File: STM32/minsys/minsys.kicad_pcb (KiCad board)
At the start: 2 copper layers, 29 parts, among them J1 USB_B_Micro, J2 ST-LINK, J3 BOOT, J4 Conn_01x20, J5 Conn_01x20, SW1 RST, U1 STM32F103C8Tx, U2 AMS1117-3.3, Y1 8MHz, Y2 32.758K

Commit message: edit pcb
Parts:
- D2: footprint LED_SMD:LED_0402_1005Metric_Pad0.77x0.64mm_HandSolder -> LED_SMD:LED_0603_1608Metric_Pad1.05x0.95mm_HandSolder
- moved R3 12.8 mm to (224.2, 76.0)
- moved R4 11.7 mm to (226.7, 35.2), turned to 180 degrees
- moved C8 4.05 mm to (234.6, 39.6)
- moved R2 3.89 mm to (230.9, 77.2), turned to -90 degrees
- moved D1 2.65 mm to (238.9, 34.3)
- moved R1 1.42 mm to (228.1, 77.2), turned to -90 degrees
- moved J2 0.88 mm to (230.2, 31.6)
- moved D2 0.28 mm to (217.4, 66.7)
- moved R5 0.26 mm to (234.9, 32.8)
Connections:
- C6 pad 1: RTCIN -> PC14
- C7 pad 1: RTCOUT -> PC15
- U1 pad 3: RTCIN -> PC14
- U1 pad 4: RTCOUT -> PC15
- Y2 pad 1: RTCIN -> PC14
- Y2 pad 2: RTCOUT -> PC15
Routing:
- net PC14: track 0.00 -> 41.1 mm
- net PC15: track 0.00 -> 36.6 mm
- net PC13: track 8.62 -> 42.6 mm
- net RTCIN: track 21.2 -> 0.00 mm
- net RTCOUT: track 18.1 -> 0.00 mm
- net Net-(J1-D-): track 0.00 -> 9.83 mm
- net SWDIO: track 0.00 -> 8.70 mm, vias 0 -> 1
- net NRST: track 15.0 -> 23.3 mm
- net SWDCLK: track 0.00 -> 7.36 mm, vias 0 -> 1
- net BOOT1: track 64.1 -> 57.2 mm
- net Net-(J1-D+): track 0.00 -> 4.02 mm
- net PA12: track 20.6 -> 23.0 mm

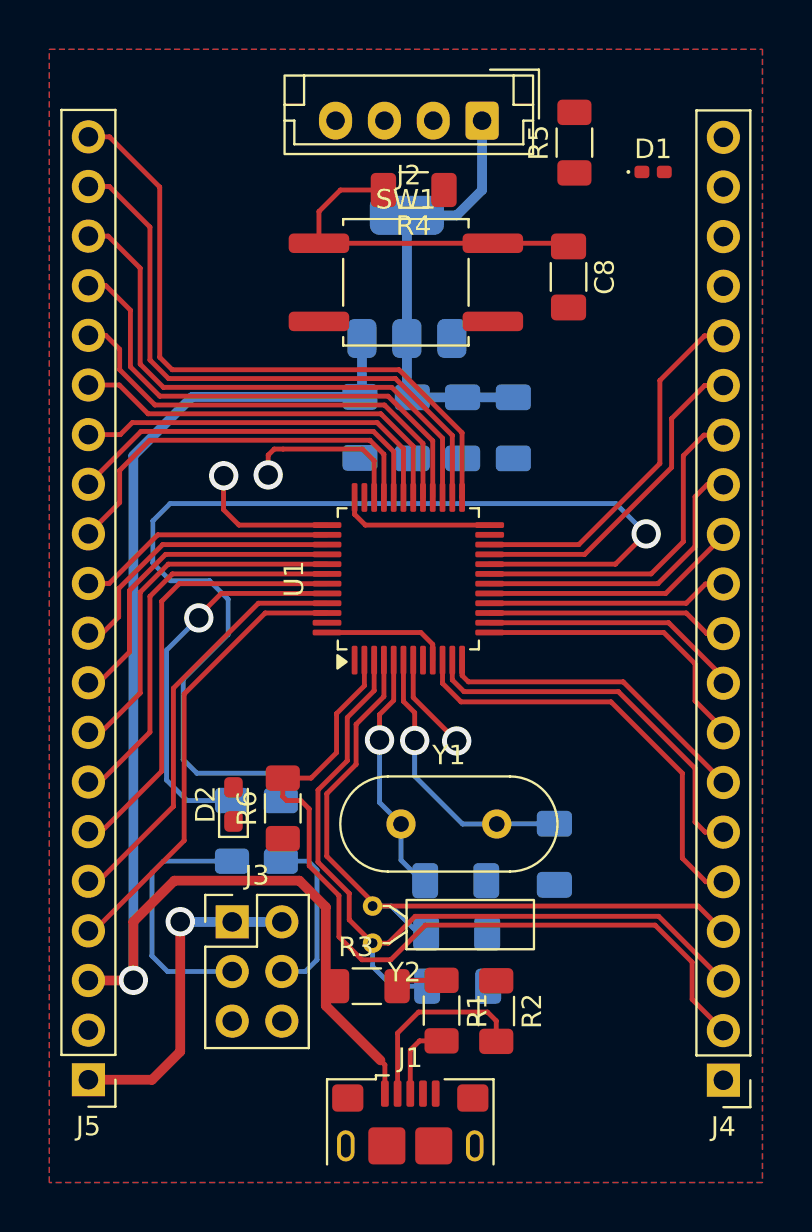
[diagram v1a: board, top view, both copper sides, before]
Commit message: add minsys.kicad(copy).pcb
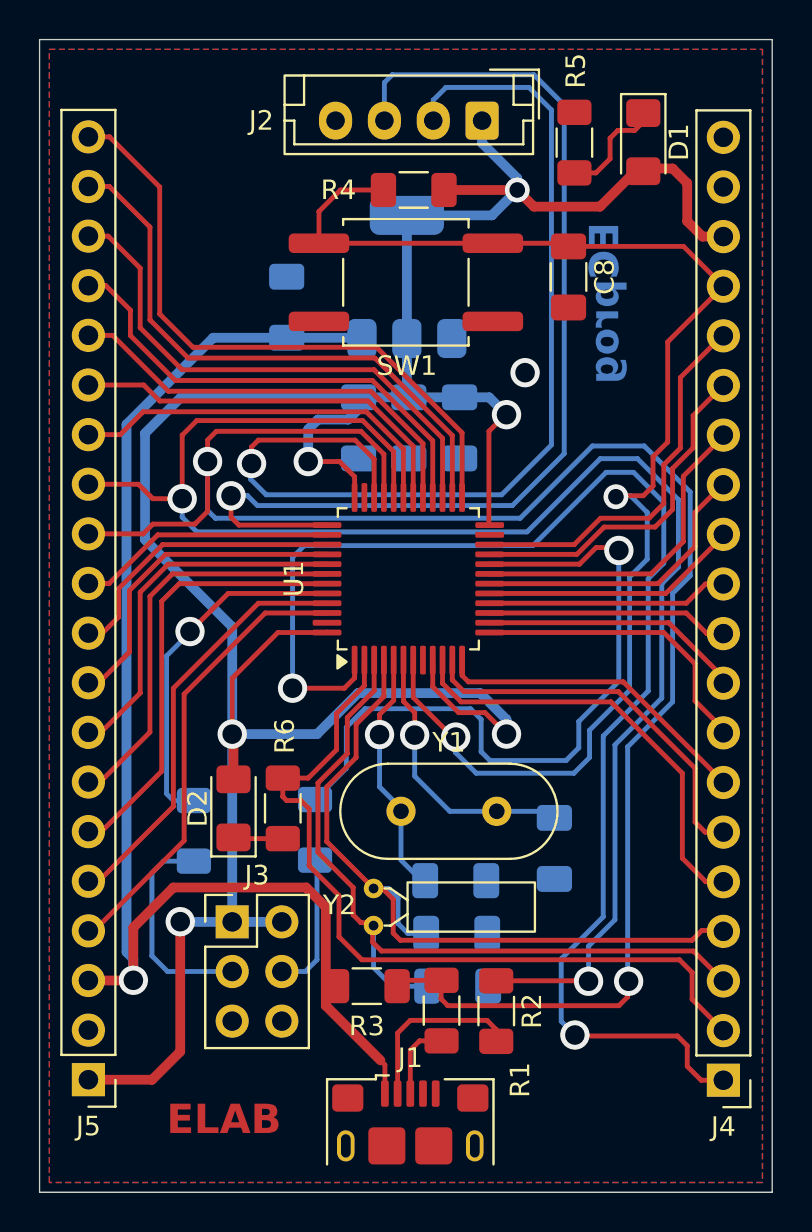
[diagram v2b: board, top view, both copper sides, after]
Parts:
- D1: footprint LED_SMD:LED_0402_1005Metric_Pad0.77x0.64mm_HandSolder -> LED_SMD:LED_1206_3216Metric_Pad1.42x1.75mm_HandSolder
- D2: footprint LED_SMD:LED_0603_1608Metric_Pad1.05x0.95mm_HandSolder -> LED_SMD:LED_1206_3216Metric_Pad1.42x1.75mm_HandSolder
- J4, J5: value Conn_01x20 -> 01x20
- moved C1 7.20 mm to (220.2, 41.2), turned to 90 degrees
- moved C2 2.75 mm to (229.0, 47.4)
- moved C3 2.75 mm to (226.4, 47.4)
- moved C9 2.75 mm to (223.8, 47.4)
- moved R8 1.95 mm to (215.4, 68.0)
- moved R7 1.75 mm to (221.6, 68.0)
- moved D1 1.61 mm to (238.4, 32.8), turned to -90 degrees
- moved Y2 0.90 mm to (224.6, 72.8)
- moved Y1 0.65 mm to (226.0, 67.0)
- moved C5 0.30 mm to (233.8, 68.9)
- moved D2 0.20 mm to (217.4, 66.8)
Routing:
- net +3.3V: track 53.3 -> 150.5 mm, vias 1 -> 6
- net VBAT: track 0.00 -> 71.3 mm, vias 0 -> 2
- net PA12: track 23.0 -> 92.8 mm, vias 0 -> 2
- net PA11: track 19.5 -> 83.3 mm, vias 0 -> 2
- net SWDCLK: track 7.36 -> 54.3 mm
- net NRST: track 23.3 -> 69.9 mm, vias 1 -> 2
- net SWDIO: track 8.70 -> 52.2 mm
- net BOOT1: track 57.2 -> 37.0 mm
- net Net-(D1-K): track 0.00 -> 5.67 mm
- net Net-(D2-K): track 0.00 -> 2.55 mm
- net PC15: track 36.6 -> 38.5 mm
- net Net-(J3-Pin_3): track 13.0 -> 11.1 mm
- net PC13: track 42.6 -> 40.7 mm
- net BOOT0: track 19.9 -> 18.2 mm
- net Net-(J3-Pin_4): track 8.68 -> 7.36 mm
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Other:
- board outline added: 37.5 x 59 mm
- board text added: "ECprog"
- board text added: "ELAB"
